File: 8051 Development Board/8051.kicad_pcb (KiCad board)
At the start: 2 copper layers, 76 parts, among them J1 Conn_01x08, J10 LCM-S01602DTR_M, J11 Conn_01x03, J12 Conn_01x08, J13 Conn_01x04, J14 PJ-102A, J15 Conn_01x01, J16 Conn_01x01, J2 Conn_02x03_Counter_Clockwise, J3 Conn_01x08, J4 Conn_01x08, J5 Conn_01x08, J6 Conn_02x03_Counter_Clockwise, J8 Conn_01x08, J9 Conn_01x08, Q1 LM7805CT_NOPB, SW1 SW_Push_Dual, SW10 SW_Push_Dual, SW11 SW_Push_Dual, SW12 SW_Push_Dual, SW13 SW_Push_Dual, SW14 SW_Push_Dual, SW15 SW_Push_Dual, SW16 SW_Push_Dual, SW17 SW_Push_Dual, SW18 SW_Push_Dual, SW19 SW_Push_Dual, SW2 SW_Push_Dual, SW20 SW_Nidec_CAS-120A1, SW3 SW_Push_Dual, SW4 SW_Push_Dual, SW5 SW_Push_Dual, SW6 SW_Push_Dual, SW7 SW_Push_Dual, SW8 SW_Push_Dual, SW9 SW_Push_Dual, U1 AT89S51-24PU, U10 2SA2222SG, U2 74F573SC, U3 74F573SC, U4 74F573SC, U5 74F573SC, U6 SC39-12EWA, U7 SC39-12EWA, U8 SC39-12EWA, U9 SC39-12EWA, Y1 ABL-11.0592MHZ-B1U-T

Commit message: layout
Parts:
- removed J2: Conn_02x03_Counter_Clockwise, Connector_PinHeader_2.54mm:PinHeader_2x03_P2.54mm_Vertical
- moved C4 121.8 mm to (57.1, 92.7), turned to -90 degrees
- moved SW1 121.1 mm to (57.7, 84.1)
- moved R1 119.1 mm to (64.8, 92.7), turned to 90 degrees
- moved J6 102.3 mm to (72.4, 82.5)
- moved C6 92.5 mm to (67.7, 101.3), turned to -90 degrees
- moved SW2 92.2 mm to (57.4, 98.8)
- moved SW3 92.0 mm to (57.4, 107.9)
- moved C7 91.0 mm to (67.7, 110.2), turned to 90 degrees
- moved H4 89.7 mm to (186.7, 161.8)
- moved H1 89.7 mm to (186.7, 145.8)
- moved H2 89.7 mm to (186.7, 151.1)
- moved H3 89.7 mm to (186.7, 156.5)
- moved C1 79.0 mm to (116.0, 67.3)
- moved J14 68.9 mm to (58.5, 138.5), turned to -90 degrees
- moved J8 60.9 mm to (119.4, 143.5)
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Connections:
- J6 pad 2: /SCK -> /P1.7
- J6 pad 3: /MISO -> /P1.6
- J6 pad 5: /MOSI -> /P1.5
- U1 pad 6: /MOSI -> /P1.5
- U1 pad 7: /MISO -> /P1.6
- U1 pad 8: /SCK -> /P1.7

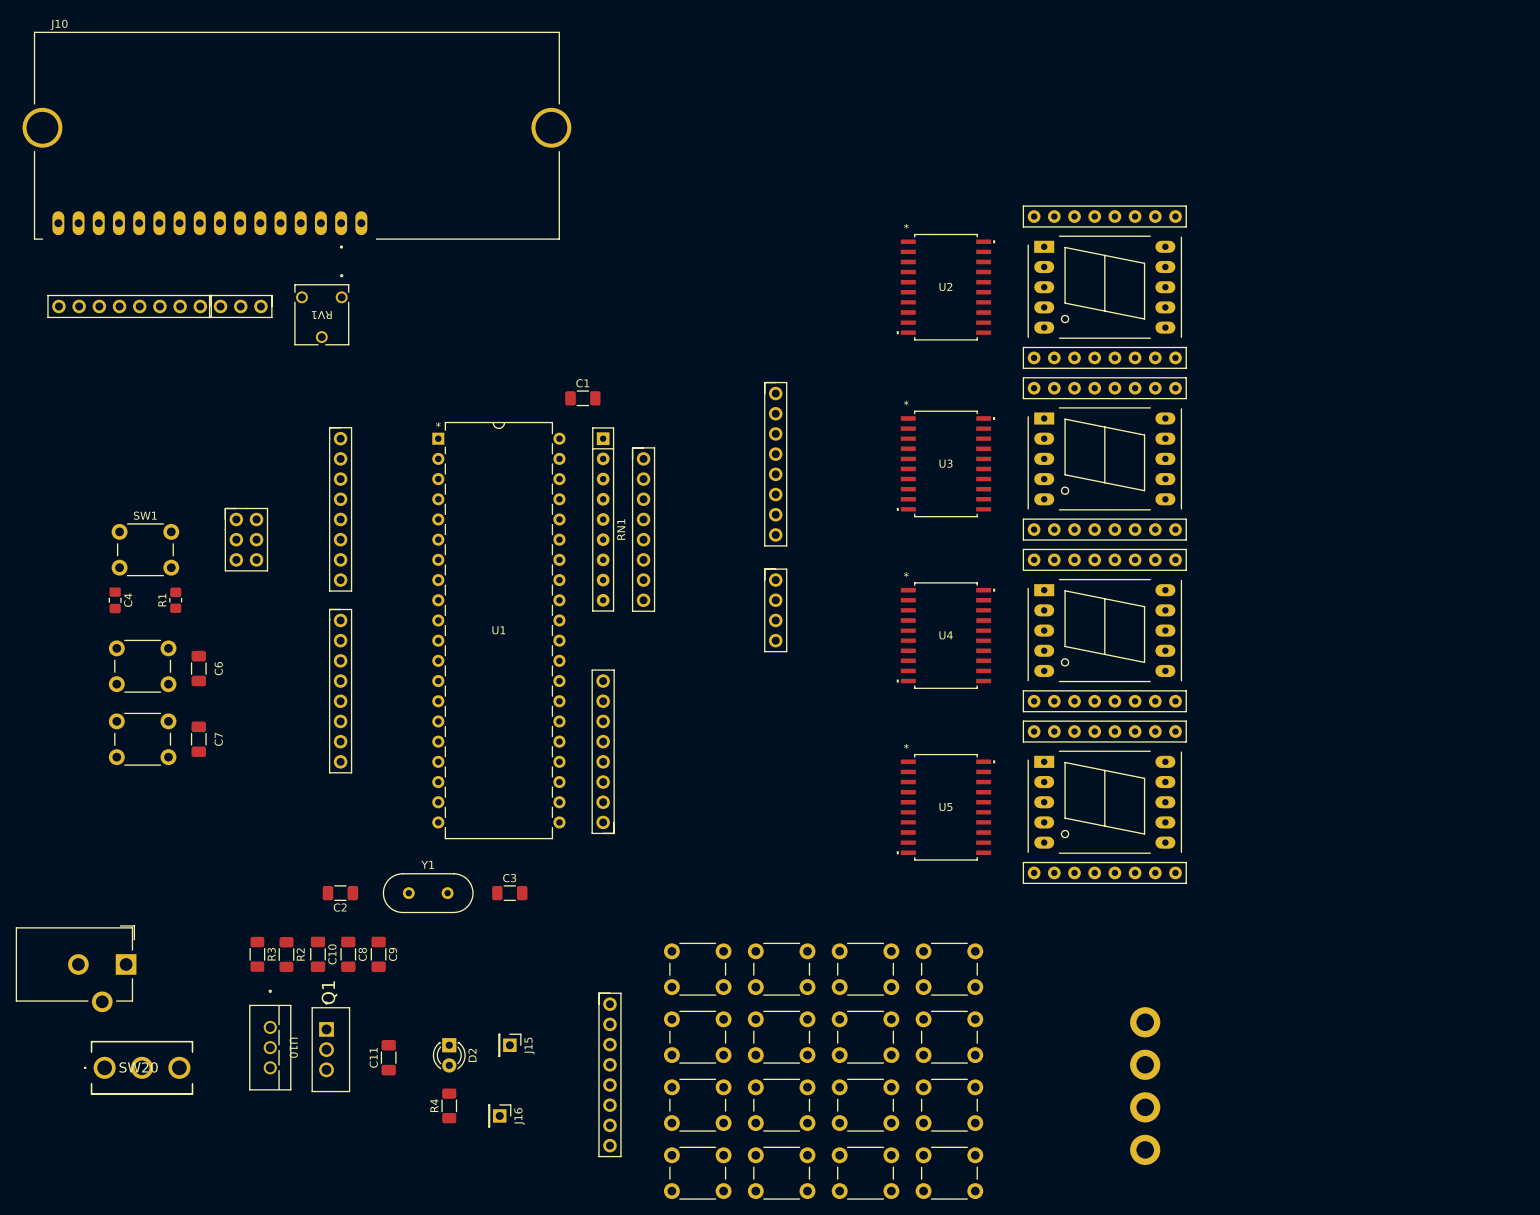
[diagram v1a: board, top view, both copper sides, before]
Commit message: 5v power plane
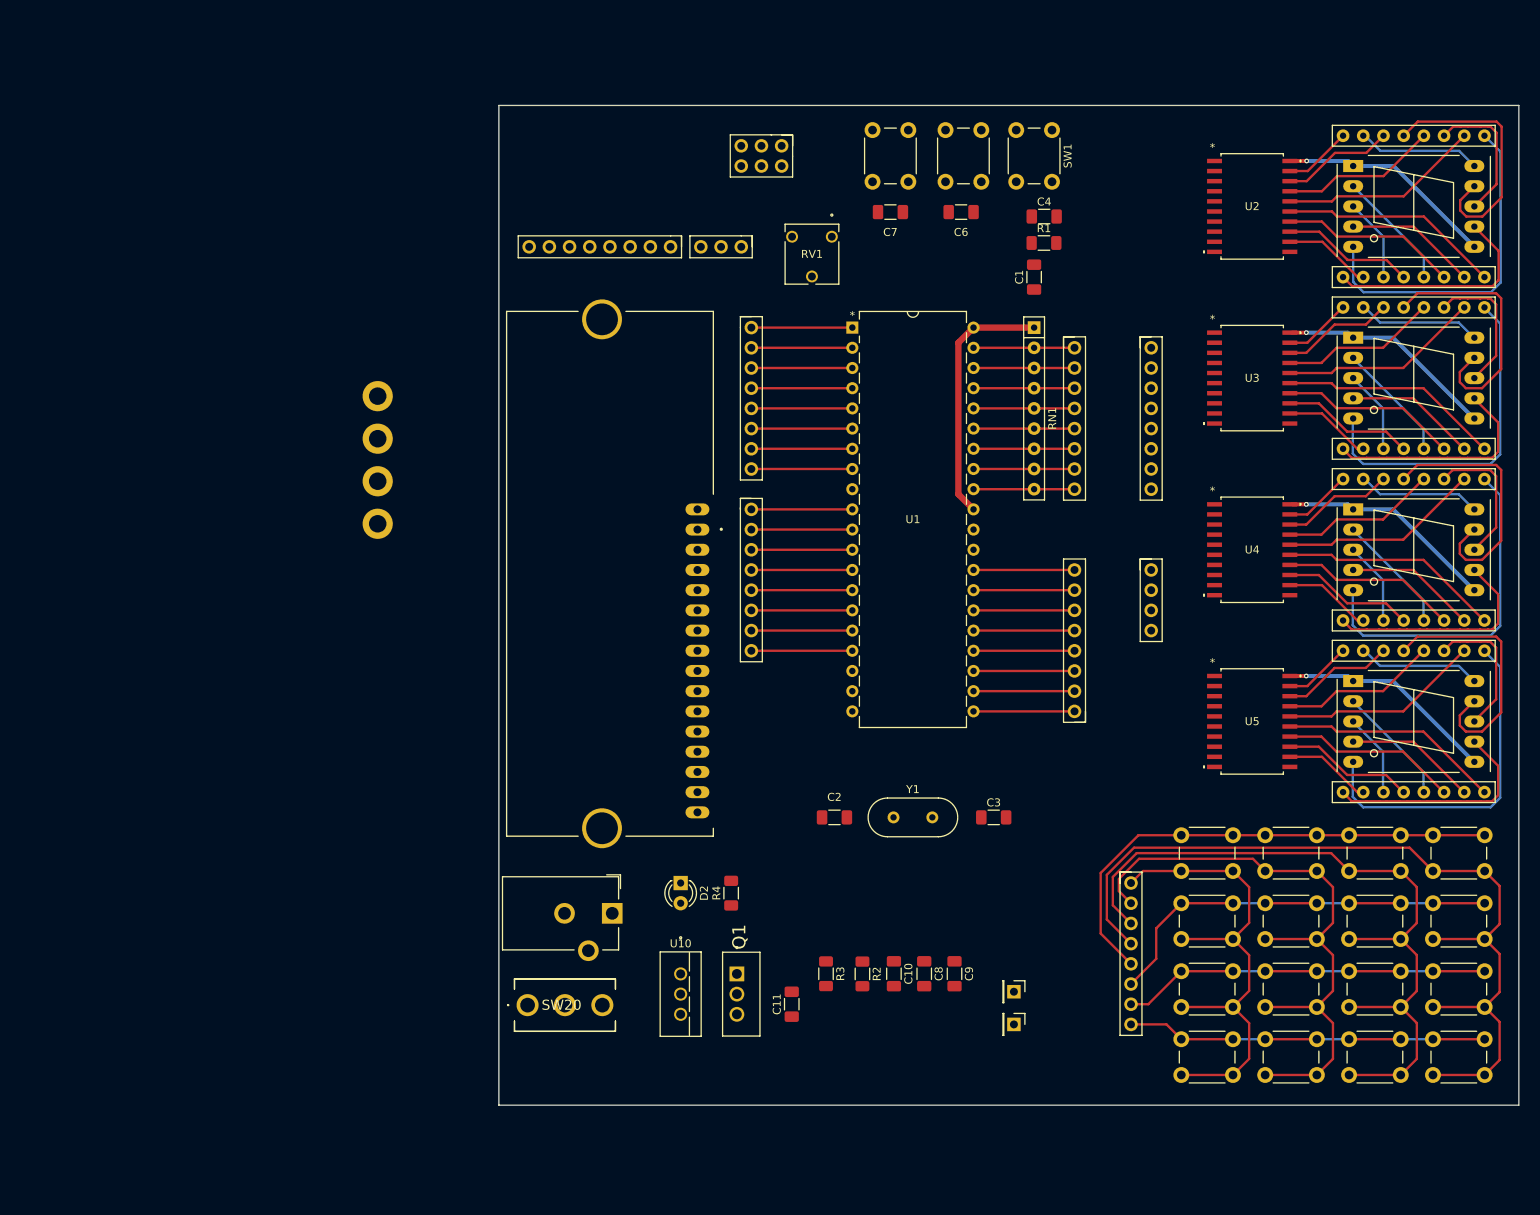
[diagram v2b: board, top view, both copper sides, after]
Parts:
- C4: footprint Capacitor_SMD:C_0805_2012Metric_Pad1.18x1.45mm_HandSolder -> Capacitor_SMD:C_1206_3216Metric_Pad1.33x1.80mm_HandSolder
- R1: footprint Resistor_SMD:R_0805_2012Metric_Pad1.20x1.40mm_HandSolder -> Resistor_SMD:R_1206_3216Metric_Pad1.30x1.75mm_HandSolder
- moved SW1 127.7 mm to (175.0, 33.6), turned to -90 degrees
- moved SW2 126.8 mm to (166.1, 33.6), turned to -90 degrees
- moved C4 126.4 mm to (174.0, 44.5), turned to 0 degrees
- moved H1 124.6 mm to (90.2, 67.0)
- moved H2 124.6 mm to (90.2, 72.4)
- moved H3 124.6 mm to (90.2, 77.7)
- moved H4 124.6 mm to (90.2, 83.1)
- moved SW3 124.2 mm to (156.9, 33.6), turned to -90 degrees
- moved R1 118.1 mm to (174.0, 47.8), turned to 0 degrees
- moved C6 111.7 mm to (163.5, 43.9), turned to 180 degrees
- moved C7 109.4 mm to (154.7, 43.9), turned to 0 degrees
- moved J6 83.1 mm to (141.0, 35.6), turned to -90 degrees
- moved C10 72.5 mm to (155.1, 139.7)
- moved C8 72.5 mm to (158.9, 139.7)
- moved C9 72.5 mm to (162.7, 139.7)
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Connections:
- U3 pad 1: GND -> (no net)
- U3 pad 10: GND -> (no net)
- U3 pad 11: Net-(J13-Pin_2) -> (no net)
- U3 pad 12: Net-(RN5-R4.1) -> (no net)
- U3 pad 13: Net-(RN5-R3.1) -> (no net)
- U3 pad 14: Net-(RN5-R2.1) -> (no net)
- U3 pad 15: Net-(RN5-R1.1) -> (no net)
- U3 pad 16: Net-(RN4-R4.1) -> (no net)
- U3 pad 17: Net-(RN4-R3.1) -> (no net)
- U3 pad 18: Net-(RN4-R2.1) -> (no net)
- U3 pad 19: Net-(RN4-R1.1) -> (no net)
- U3 pad 2: Net-(J12-Pin_1) -> (no net)
- U3 pad 20: +5V -> (no net)
- U3 pad 3: Net-(J12-Pin_2) -> (no net)
- U3 pad 4: Net-(J12-Pin_3) -> (no net)
- U3 pad 5: Net-(J12-Pin_4) -> (no net)
- U3 pad 6: Net-(J12-Pin_5) -> (no net)
- U3 pad 7: Net-(J12-Pin_6) -> (no net)
- U3 pad 8: Net-(J12-Pin_7) -> (no net)
- U3 pad 9: Net-(J12-Pin_8) -> (no net)
- U4 pad 1: GND -> (no net)
- U4 pad 10: GND -> (no net)
- U4 pad 11: Net-(J13-Pin_3) -> (no net)
- U4 pad 12: Net-(RN7-R4.1) -> (no net)
- U4 pad 13: Net-(RN7-R3.1) -> (no net)
- U4 pad 14: Net-(RN7-R2.1) -> (no net)
- U4 pad 15: Net-(RN7-R1.1) -> (no net)
- U4 pad 16: Net-(RN6-R4.1) -> (no net)
- U4 pad 17: Net-(RN6-R3.1) -> (no net)
- U4 pad 18: Net-(RN6-R2.1) -> (no net)
- U4 pad 19: Net-(RN6-R1.1) -> (no net)
- U4 pad 2: Net-(J12-Pin_1) -> (no net)
- U4 pad 20: +5V -> (no net)
- U4 pad 3: Net-(J12-Pin_2) -> (no net)
- U4 pad 4: Net-(J12-Pin_3) -> (no net)
- U4 pad 5: Net-(J12-Pin_4) -> (no net)
- U4 pad 6: Net-(J12-Pin_5) -> (no net)
- U4 pad 7: Net-(J12-Pin_6) -> (no net)
- U4 pad 8: Net-(J12-Pin_7) -> (no net)
- U4 pad 9: Net-(J12-Pin_8) -> (no net)
- U5 pad 1: GND -> (no net)
- U5 pad 10: GND -> (no net)
- U5 pad 11: Net-(J13-Pin_4) -> (no net)
- U5 pad 12: Net-(RN9-R4.1) -> (no net)
- U5 pad 13: Net-(RN9-R3.1) -> (no net)
- U5 pad 14: Net-(RN9-R2.1) -> (no net)
- U5 pad 15: Net-(RN9-R1.1) -> (no net)
- U5 pad 16: Net-(RN8-R4.1) -> (no net)
- U5 pad 17: Net-(RN8-R3.1) -> (no net)
- U5 pad 18: Net-(RN8-R2.1) -> (no net)
- U5 pad 19: Net-(RN8-R1.1) -> (no net)
- U5 pad 2: Net-(J12-Pin_1) -> (no net)
- U5 pad 20: +5V -> (no net)
- U5 pad 3: Net-(J12-Pin_2) -> (no net)
- U5 pad 4: Net-(J12-Pin_3) -> (no net)
- U5 pad 5: Net-(J12-Pin_4) -> (no net)
- U5 pad 6: Net-(J12-Pin_5) -> (no net)
- U5 pad 7: Net-(J12-Pin_6) -> (no net)
- U5 pad 8: Net-(J12-Pin_7) -> (no net)
- U5 pad 9: Net-(J12-Pin_8) -> (no net)
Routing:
- net +5V: track 0.00 -> 141.7 mm, vias 0 -> 4
- net /KEYPAD_HEX/C4: track 0.00 -> 109.9 mm
- net /KEYPAD_HEX/C3: track 0.00 -> 95.3 mm
- net /KEYPAD_HEX/C2: track 0.00 -> 80.5 mm
- net /KEYPAD_HEX/C1: track 0.00 -> 63.7 mm
- net /KEYPAD_HEX/R1: track 0.00 -> 63.3 mm
- net /KEYPAD_HEX/R2: track 0.00 -> 50.9 mm
- net /KEYPAD_HEX/R3: track 0.00 -> 46.2 mm
- net /KEYPAD_HEX/R4: track 0.00 -> 45.2 mm
- net Net-(RN6-R4.2): track 0.00 -> 43.3 mm
- net Net-(RN2-R4.2): track 0.00 -> 43.3 mm
- net Net-(RN8-R4.2): track 0.00 -> 43.3 mm
- net Net-(RN4-R4.2): track 0.00 -> 43.3 mm
- net Net-(RN2-R2.2): track 0.00 -> 32.5 mm
- net Net-(RN4-R2.2): track 0.00 -> 32.5 mm
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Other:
- board outline added: 128.3 x 125.7 mm

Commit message: dev board gerbers
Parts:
- removed H1, H2, H3, H4: MountingHole, MountingHole:MountingHole_2.2mm_M2_DIN965_Pad
- added G***: LOGO, LOGO, F.Cu at (168.7, 138.2)
- added G***: LOGO, LOGO, B.Cu at (170.2, 93.3)
- added kibuzzard-68D8BB38: G***, kibuzzard-68D8BB38, F.Cu at (122.2, 37.8)
- added kibuzzard-68D8BC51: G***, kibuzzard-68D8BC51, F.Cu at (167.6, 152.7)
- moved RV1 65.0 mm to (141.5, 111.7), turned to 90 degrees
- moved C4 31.2 mm to (142.8, 43.9)
- moved R1 31.2 mm to (142.8, 47.7), turned to 180 degrees
- moved SW1 29.2 mm to (145.8, 33.6)
- moved C9 25.1 mm to (139.7, 149.6)
- moved R2 25.0 mm to (126.2, 142.0), turned to 90 degrees
- moved C7 22.9 mm to (177.5, 43.8)
- moved SW3 22.2 mm to (179.1, 33.6)
- moved C10 21.6 mm to (135.8, 149.6)
- moved C3 20.4 mm to (147.3, 118.7), turned to 180 degrees
- moved C2 19.8 mm to (167.3, 118.7), turned to 0 degrees
- moved J6 19.1 mm to (160.0, 37.3)
- moved C8 18.3 mm to (143.5, 149.6)
- moved J15 17.8 mm to (154.3, 134.0)
- moved J16 16.0 mm to (154.3, 148.0)
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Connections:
- U3 pad 1: (no net) -> GND
- U3 pad 10: (no net) -> GND
- U3 pad 11: (no net) -> Net-(J13-Pin_2)
- U3 pad 12: (no net) -> Net-(RN5-R4.1)
- U3 pad 13: (no net) -> Net-(RN5-R3.1)
- U3 pad 14: (no net) -> Net-(RN5-R2.1)
- U3 pad 15: (no net) -> Net-(RN5-R1.1)
- U3 pad 16: (no net) -> Net-(RN4-R4.1)
- U3 pad 17: (no net) -> Net-(RN4-R3.1)
- U3 pad 18: (no net) -> Net-(RN4-R2.1)
- U3 pad 19: (no net) -> Net-(RN4-R1.1)
- U3 pad 2: (no net) -> Net-(J12-Pin_1)
- U3 pad 20: (no net) -> +5V
- U3 pad 3: (no net) -> Net-(J12-Pin_2)
- U3 pad 4: (no net) -> Net-(J12-Pin_3)
- U3 pad 5: (no net) -> Net-(J12-Pin_4)
- U3 pad 6: (no net) -> Net-(J12-Pin_5)
- U3 pad 7: (no net) -> Net-(J12-Pin_6)
- U3 pad 8: (no net) -> Net-(J12-Pin_7)
- U3 pad 9: (no net) -> Net-(J12-Pin_8)
- U4 pad 1: (no net) -> GND
- U4 pad 10: (no net) -> GND
- U4 pad 11: (no net) -> Net-(J13-Pin_3)
- U4 pad 12: (no net) -> Net-(RN7-R4.1)
- U4 pad 13: (no net) -> Net-(RN7-R3.1)
- U4 pad 14: (no net) -> Net-(RN7-R2.1)
- U4 pad 15: (no net) -> Net-(RN7-R1.1)
- U4 pad 16: (no net) -> Net-(RN6-R4.1)
- U4 pad 17: (no net) -> Net-(RN6-R3.1)
- U4 pad 18: (no net) -> Net-(RN6-R2.1)
- U4 pad 19: (no net) -> Net-(RN6-R1.1)
- U4 pad 2: (no net) -> Net-(J12-Pin_1)
- U4 pad 20: (no net) -> +5V
- U4 pad 3: (no net) -> Net-(J12-Pin_2)
- U4 pad 4: (no net) -> Net-(J12-Pin_3)
- U4 pad 5: (no net) -> Net-(J12-Pin_4)
- U4 pad 6: (no net) -> Net-(J12-Pin_5)
- U4 pad 7: (no net) -> Net-(J12-Pin_6)
- U4 pad 8: (no net) -> Net-(J12-Pin_7)
- U4 pad 9: (no net) -> Net-(J12-Pin_8)
- U5 pad 1: (no net) -> GND
- U5 pad 10: (no net) -> GND
- U5 pad 11: (no net) -> Net-(J13-Pin_4)
- U5 pad 12: (no net) -> Net-(RN9-R4.1)
- U5 pad 13: (no net) -> Net-(RN9-R3.1)
- U5 pad 14: (no net) -> Net-(RN9-R2.1)
- U5 pad 15: (no net) -> Net-(RN9-R1.1)
- U5 pad 16: (no net) -> Net-(RN8-R4.1)
- U5 pad 17: (no net) -> Net-(RN8-R3.1)
- U5 pad 18: (no net) -> Net-(RN8-R2.1)
- U5 pad 19: (no net) -> Net-(RN8-R1.1)
- U5 pad 2: (no net) -> Net-(J12-Pin_1)
- U5 pad 20: (no net) -> +5V
- U5 pad 3: (no net) -> Net-(J12-Pin_2)
- U5 pad 4: (no net) -> Net-(J12-Pin_3)
- U5 pad 5: (no net) -> Net-(J12-Pin_4)
- U5 pad 6: (no net) -> Net-(J12-Pin_5)
- U5 pad 7: (no net) -> Net-(J12-Pin_6)
- U5 pad 8: (no net) -> Net-(J12-Pin_7)
- U5 pad 9: (no net) -> Net-(J12-Pin_8)
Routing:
- net Net-(J12-Pin_4): track 0.00 -> 87.0 mm, vias 0 -> 3
- net Net-(J12-Pin_3): track 0.00 -> 86.4 mm, vias 0 -> 4
- net Net-(J12-Pin_8): track 0.00 -> 84.4 mm, vias 0 -> 5
- net Net-(J12-Pin_6): track 0.00 -> 84.1 mm, vias 0 -> 4
- net Net-(J12-Pin_1): track 0.00 -> 83.2 mm, vias 0 -> 3
- net Net-(J12-Pin_7): track 0.00 -> 82.5 mm, vias 0 -> 4
- net /LCD/D7: track 0.00 -> 81.4 mm
- net Net-(J12-Pin_2): track 0.00 -> 80.8 mm, vias 0 -> 4
- net Net-(J12-Pin_5): track 0.00 -> 80.7 mm, vias 0 -> 4
- net /LCD/D6: track 0.00 -> 78.9 mm
- net /RST: track 0.00 -> 78.0 mm
- net /LCD/D5: track 0.00 -> 76.3 mm
- net /LCD/D4: track 0.00 -> 73.8 mm
- net GND: track 0.00 -> 72.9 mm, vias 0 -> 41
- net /LCD/D3: track 0.00 -> 71.3 mm
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- added copper zone on F.Cu, net +5V
- added copper zone on B.Cu, net GND
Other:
- board text added: "2SA2222SG"
- board text added: "601030"
- board text added: "7-20V"
- board text added: "74F573SC"
- board text added: "7_SEG_DISP"
- board text added: "ABL-11.0592MHZ-B1U-T"
- board text added: "AT89S51"
- board text added: "C1 C2 C3 C4 R1 R2 R3 R4"
- board text added: "D7 D6 D5 D4 D3 D2 D1 D0"
- board text added: "E RW RS"
- board text added: "GND 5V"
- board text added: "GND MOSI VCC"
- board text added: "KEYPAD_HEX"
- board text added: "LCD"
- board text added: "LCM-S01602DTR/M"
- board text added: "LM7805CT"
- board text added: "P0.0 P0.1 P0.2 P0.3 P0.4 P0.5 P0.6 P0.7 P2.7 P2.6 P2.5 P2.4 P2.3 P2.2 P2.1 P2.0"
- board text added: "P1.0 P1.1 P1.2 P1.3 P1.4 P1.5 P1.6 P1.7 P3.0 P3.1 P3.2 P3.3 P3.4 P3.5 P3.6 P3.7"
- board text added: "Port 0"
- board text added: "Port 1"
- board text added: "Port 2"
- board text added: "Port 3"
- board text added: "RESET"
- board text added: "RST SCK MISO"
